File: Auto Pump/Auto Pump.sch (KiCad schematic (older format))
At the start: 14 parts

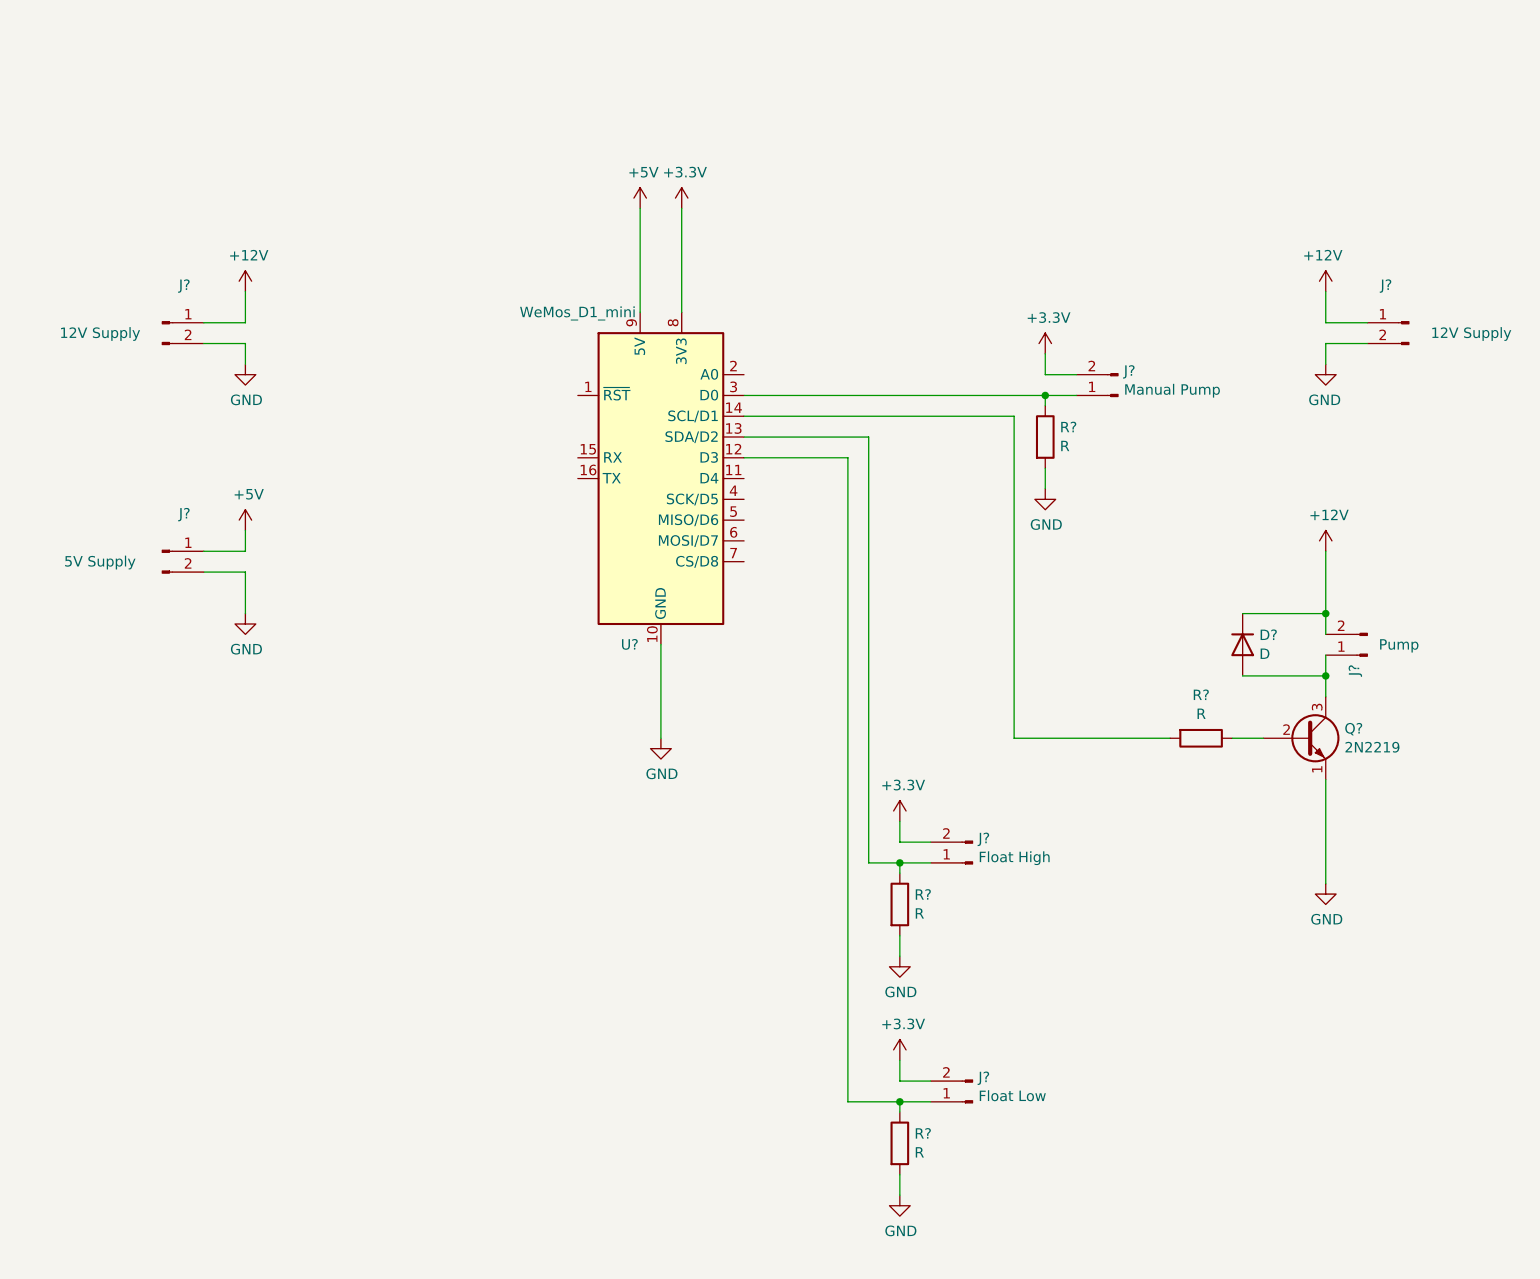
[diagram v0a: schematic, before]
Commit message: First pass at arduino code using Homie standard
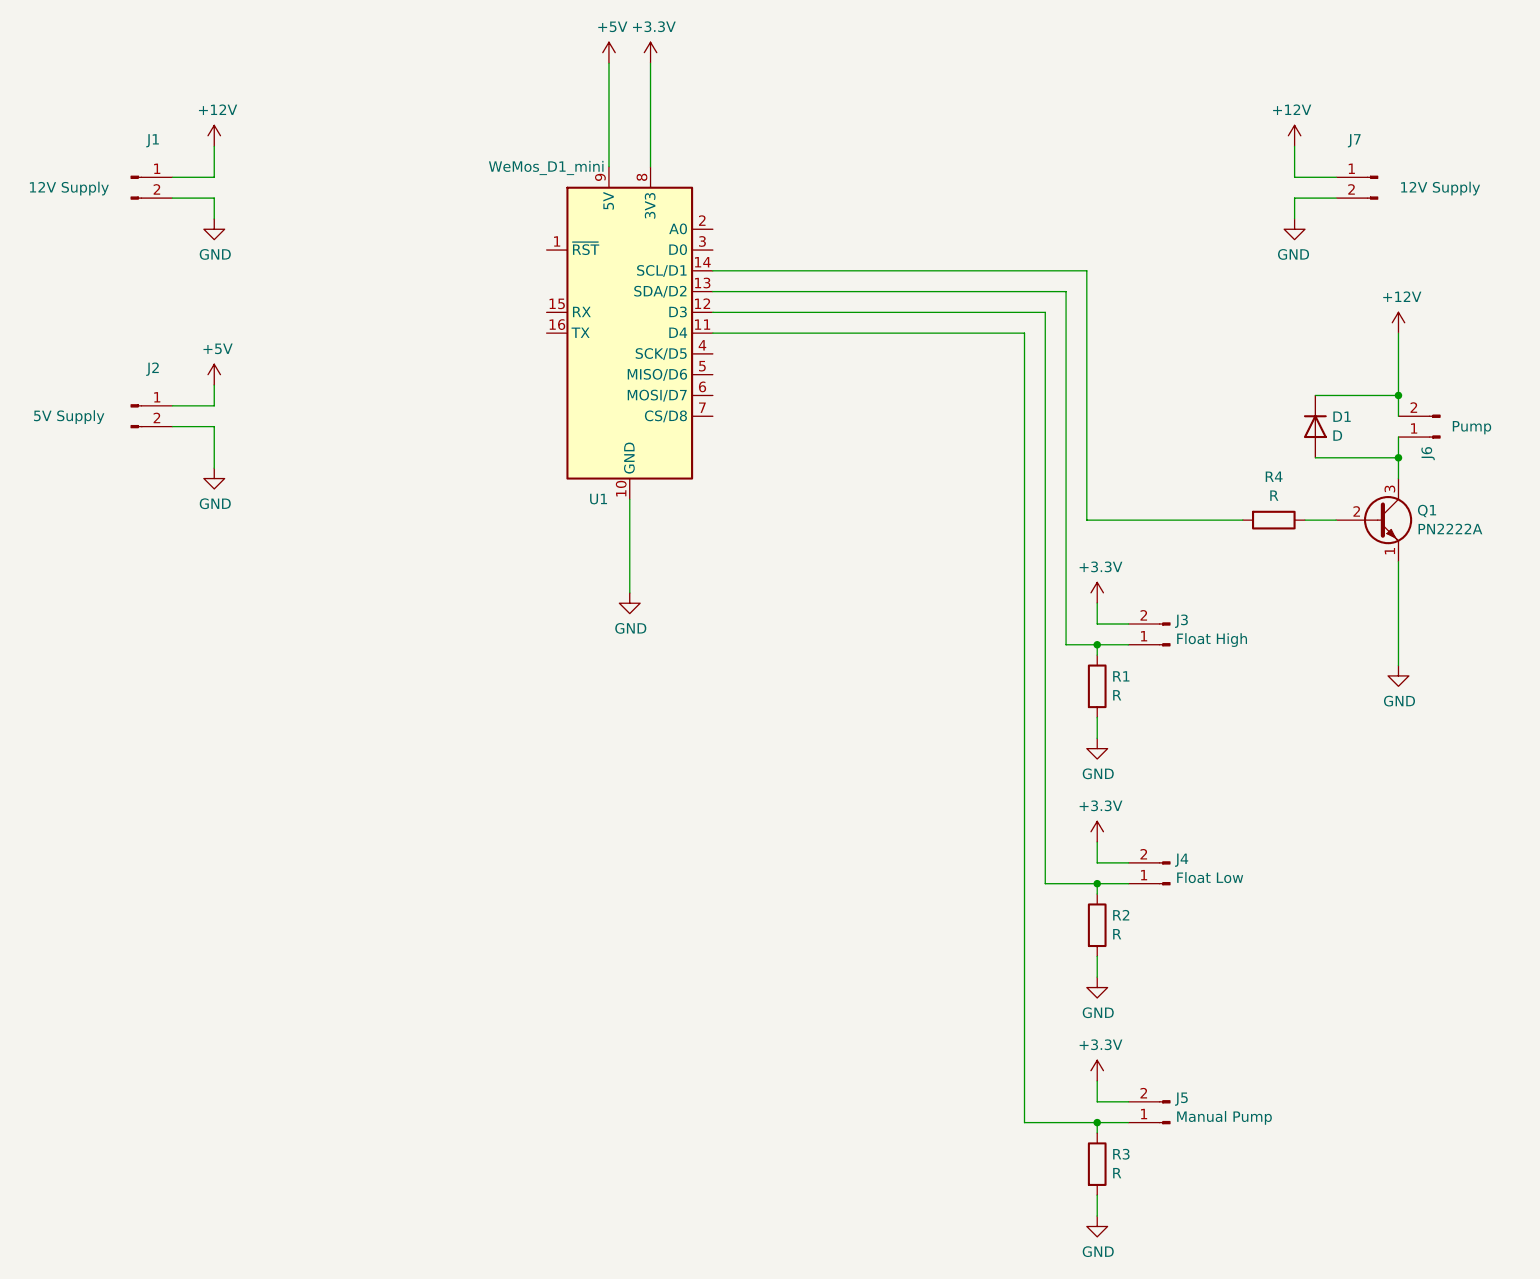
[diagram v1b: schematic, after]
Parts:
- removed Q?: 2N2219, Package_TO_SOT_THT:TO-39-3, symbol Transistor_BJT:2N2219
- added Q1: PN2222A, Package_TO_SOT_THT:TO-92_Inline, symbol Transistor_BJT:PN2222A
- D1: renamed from D?; footprint (none) -> Diode_THT:D_A-405_P12.70mm_Horizontal
- J1, J2, J3, J4, J5, J6, J7: renamed from J?; footprint (none) -> Connector_PinHeader_2.54mm:PinHeader_1x02_P2.54mm_Vertical
- R1, R2, R3, R4: renamed from R?; footprint (none) -> Resistor_THT:R_Axial_DIN0309_L9.0mm_D3.2mm_P12.70mm_Horizontal
- gave numbers to parts that had none: 1
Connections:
- net GND: now also Q1.1 (E)
- net at U1.11 (D4): now also J5.1 (Pin_1), R3.1
- net at D1.2 (A), J6.1 (Pin_1): now also Q1.3 (C)
- net at R4.1: now also Q1.2 (B)
- now unconnected: U1.3 (D0)
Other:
- moved on the sheet: D1, J1, J2, J3, J4, J5, J6, J7, R1, R2, R3, R4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
